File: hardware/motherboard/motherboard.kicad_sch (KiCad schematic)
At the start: 87 parts, among them J1 IMU Connector, J2 JST-VH, J3 JST-VH, J4 JST-PH, J5 USB C 2.0, J6 Conn_01x03_Pin, Q1 TSM7P06CP_ROG, Q2 TSM7P06CP_ROG, Q3 AO3400A, Q5 AO3400A, SW1 A, SW10 Right, SW11 Left, SW12 Up, SW13 Reset, SW2 B, SW3 X, SW4 Y, SW5 LB, SW6 RB, SW7 Start, SW8 Select, SW9 Down, U1 ESP32-S3-WROOM-1, U2 MCP73831-2-OT, U3 TPS75533KTTRG3, U4 TLV75709PDBV

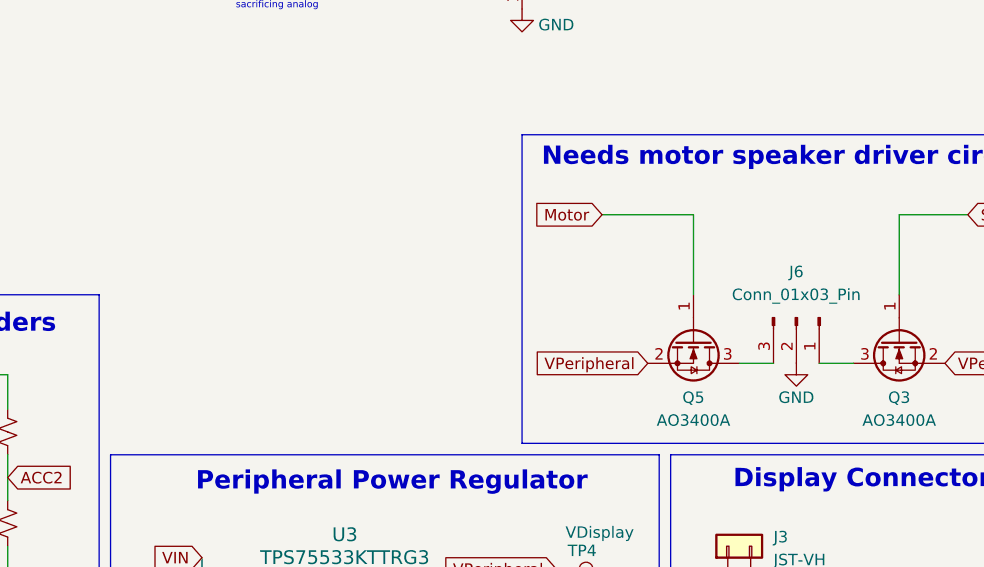
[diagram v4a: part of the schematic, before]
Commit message: Updated Mounting Holes
Made display holes M3

Matching hole pattern on motherboard to mount display.

Distributed 4, M3 mounting holes throuhout motherboard
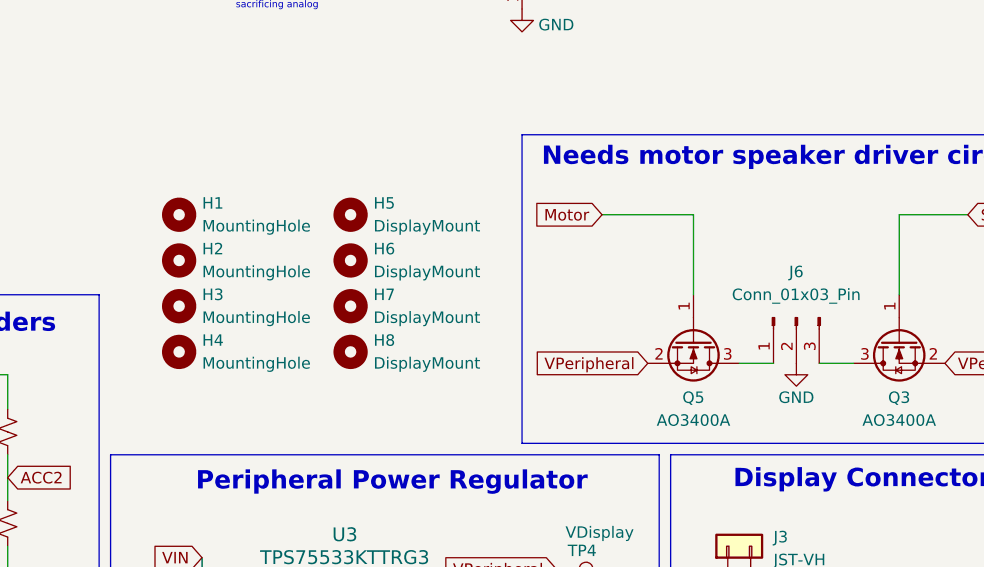
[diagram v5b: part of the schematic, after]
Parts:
- added H1, H2, H3, H4: MountingHole, MountingHole:MountingHole_3.2mm_M3_Pad, symbol Mechanical:MountingHole
- added H5, H6, H7, H8: DisplayMount, MountingHole:MountingHole_3.2mm_M3_Pad, symbol Mechanical:MountingHole
- J6: footprint Connector_JST:JST_EH_S3B-EH_1x03_P2.50mm_Horizontal -> Connector_JST:JST_PH_S3B-PH-K_1x03_P2.00mm_Horizontal
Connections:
- net at J6.1 (Pin_1): now also Q5.3 (D); no longer Q3.3 (D)
- net at J6.3 (Pin_3): now also Q3.3 (D); no longer Q5.3 (D)
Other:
- moved on the sheet: J6

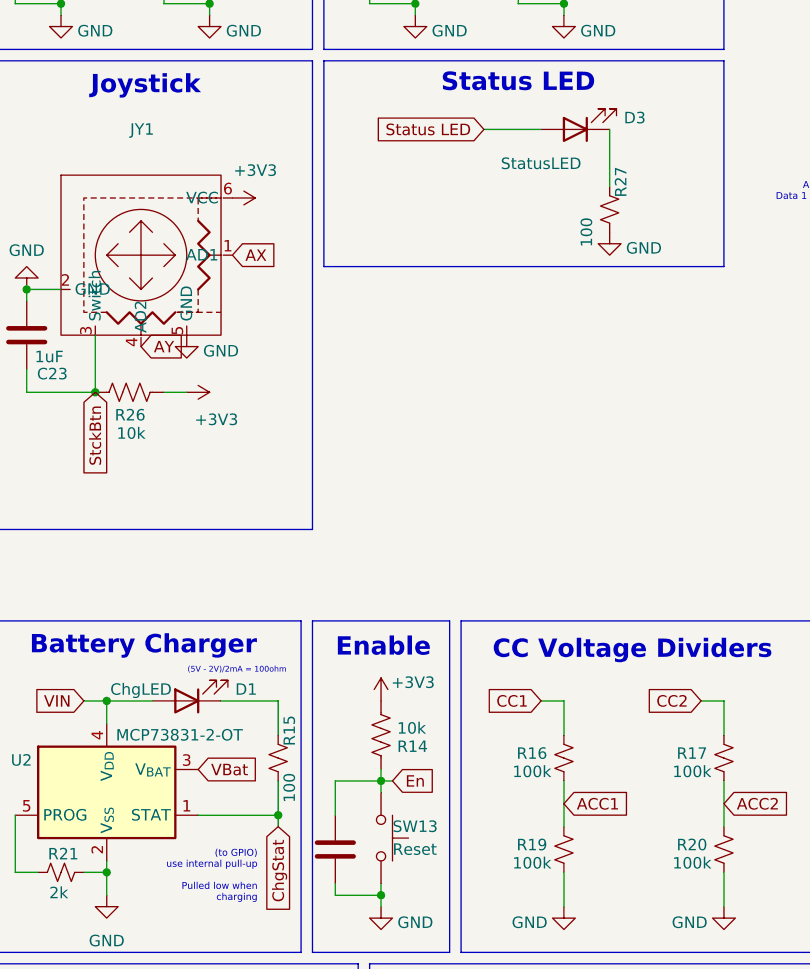
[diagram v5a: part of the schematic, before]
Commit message: Updated Motherboard and Minor Display Changes
Updated Joystick Position, Moved Display Board Port

other small fixes
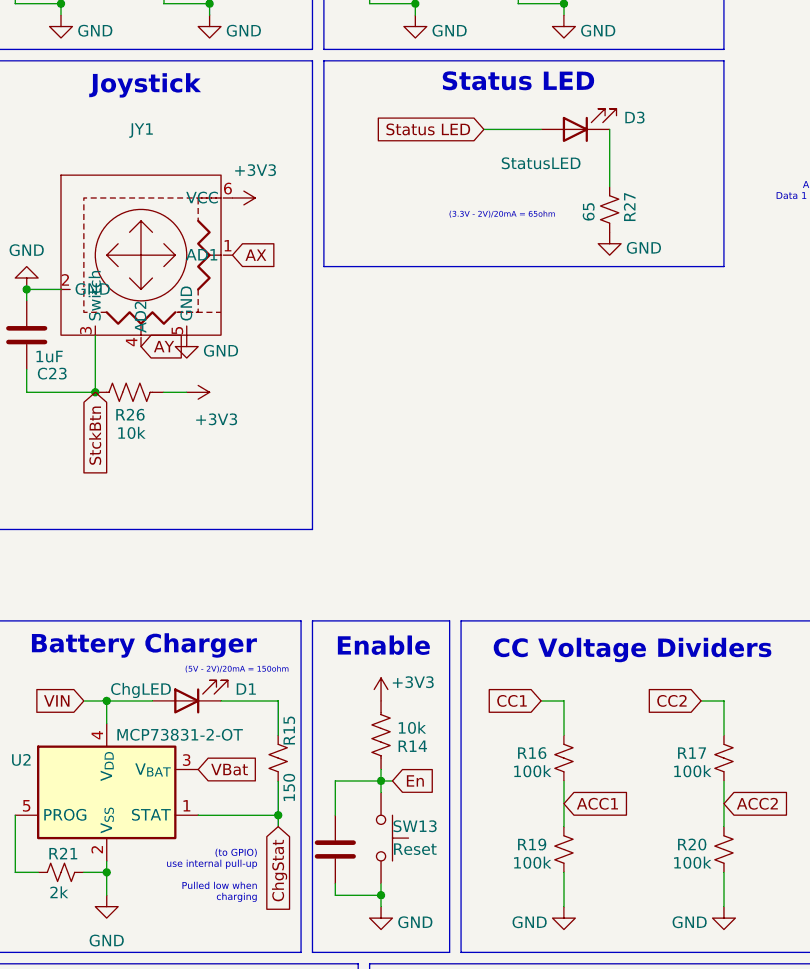
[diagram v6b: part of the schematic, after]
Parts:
- D1, D3: footprint LED_SMD:LED_1206_3216Metric -> LED_SMD:LED_1206_3216Metric_Pad1.42x1.75mm_HandSolder
- R15: value 100 -> 150
- R27: value 100 -> 65
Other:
- note added: "(3.3V - 2V)/20mA = 65ohm"
- note added: "(5V - 2V)/20mA = 150ohm"
- note removed: "(5V - 2V)/2mA = 100ohm"
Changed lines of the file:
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@@
 		)
 	)
-	(text "(5V - 2V)/2mA = 100ohm"
+	(text "(5V - 2V)/20mA = 150ohm"
 		(exclude_from_sim no)
 		(at 110.998 118.618 0)
@@
 		)
 	)
+	(text "(3.3V - 2V)/20mA = 65ohm"
+		(exclude_from_sim no)
+		(at 140.462 68.072 0)
+		(effects
+			(font
+				(size 0.635 0.635)
+			)
+		)
+	)
 	(text "A/B/X/Y"
 		(exclude_from_sim no)
@@
 			)
 		)
-		(property "Footprint" "LED_SMD:LED_1206_3216Metric"
+		(property "Footprint" "LED_SMD:LED_1206_3216Metric_Pad1.42x1.75mm_HandSolder"
 			(at 105.41 121.92 0)
 			(effects
@@
 			)
 		)
-		(property "Value" "100"
+		(property "Value" "150"
 			(at 116.84 131.572 90)
 			(effects
@@
 		(dnp no)
 		(property "Reference" "R27"
-			(at 153.67 64.262 90)
+			(at 154.686 67.056 90)
 			(effects
 				(font
@@
 			)
 		)
-		(property "Value" "100"
-			(at 149.86 69.85 90)
+		(property "Value" "65"
+			(at 150.114 67.564 90)
 			(effects
 				(font
@@
 			)
 		)
-		(property "Footprint" "LED_SMD:LED_1206_3216Metric"
+		(property "Footprint" "LED_SMD:LED_1206_3216Metric_Pad1.42x1.75mm_HandSolder"
 			(at 148.59 58.42 0)
 			(effects

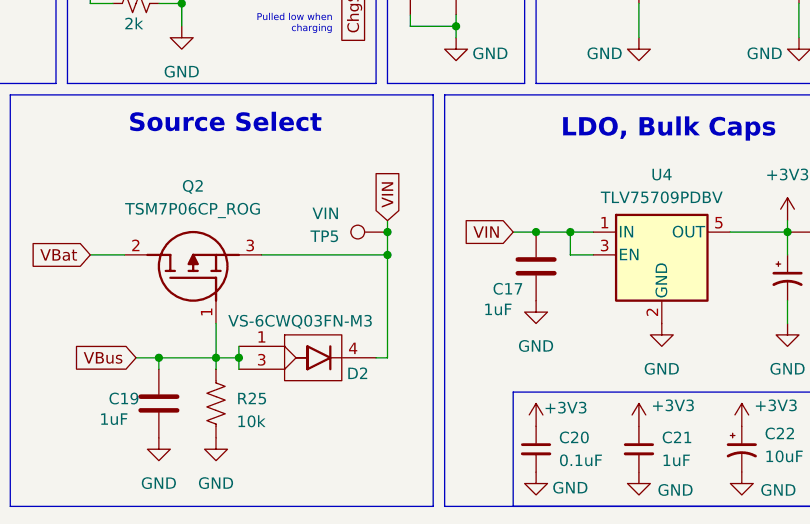
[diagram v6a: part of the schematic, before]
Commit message: ERC and DRC Checks
Made slight modifications to schematics and layouts to ensure ERCs and DRCs pass on both boards.

Made some exclusions for irrelevant warnings.
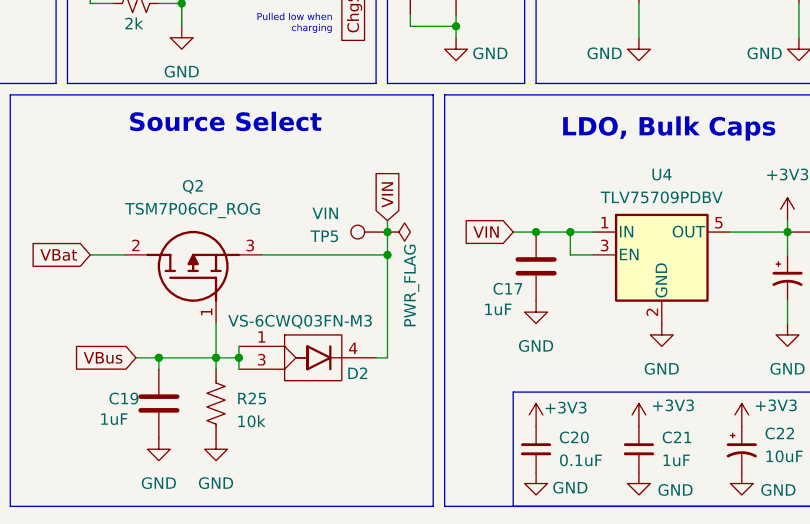
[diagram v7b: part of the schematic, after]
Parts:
- U3: footprint esp32_handheld:KTT5_6P22X6P86 -> KTT5_6P22X6P86
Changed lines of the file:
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@@
 	)
 	(symbol
+		(lib_id "power:PWR_FLAG")
+		(at 119.38 166.37 270)
+		(unit 1)
+		(exclude_from_sim no)
+		(in_bom yes)
+		(on_board yes)
+		(dnp no)
+		(property "Reference" "#FLG01"
+			(at 121.285 166.37 0)
+			(effects
+				(font
+					(size 1.27 1.27)
+				)
+				(hide yes)
+			)
+		)
+		(property "Value" "PWR_FLAG"
+			(at 121.92 167.64 0)
+			(effects
+				(font
+					(size 1.27 1.27)
+				)
+				(justify left)
+			)
+		)
+		(property "Footprint" ""
+			(at 119.38 166.37 0)
+			(effects
+				(font
+					(size 1.27 1.27)
+				)
+				(hide yes)
+			)
+		)
+		(property "Datasheet" "~"
+			(at 119.38 166.37 0)
+			(effects
+				(font
+					(size 1.27 1.27)
+				)
+				(hide yes)
+			)
+		)
+		(property "Description" "Special symbol for telling ERC where power comes from"
+			(at 119.38 166.37 0)
+			(effects
+				(font
+					(size 1.27 1.27)
+				)
+				(hide yes)
+			)
+		)
+		(pin "1"
+		)
+		(instances
+			(project ""
+				(path "/4bd92664-563a-4440-acf2-e22b0a15db62"
+					(reference "#FLG01")
+					(unit 1)
+				)
+			)
+		)
+	)
+	(symbol
 		(lib_id "power:GND")
 		(at 135.89 173.99 0)
@@
 	)
 	(symbol
+		(lib_name "Conn_01x02_1")
 		(lib_id "Connector_Generic:Conn_01x02")
 		(at 20.32 121.92 270)
@@
 			)
 		)
-		(property "Footprint" "esp32_handheld:KTT5_6P22X6P86"
+		(property "Footprint" "KTT5_6P22X6P86"
 			(at 183.896 131.064 0)
 			(effects

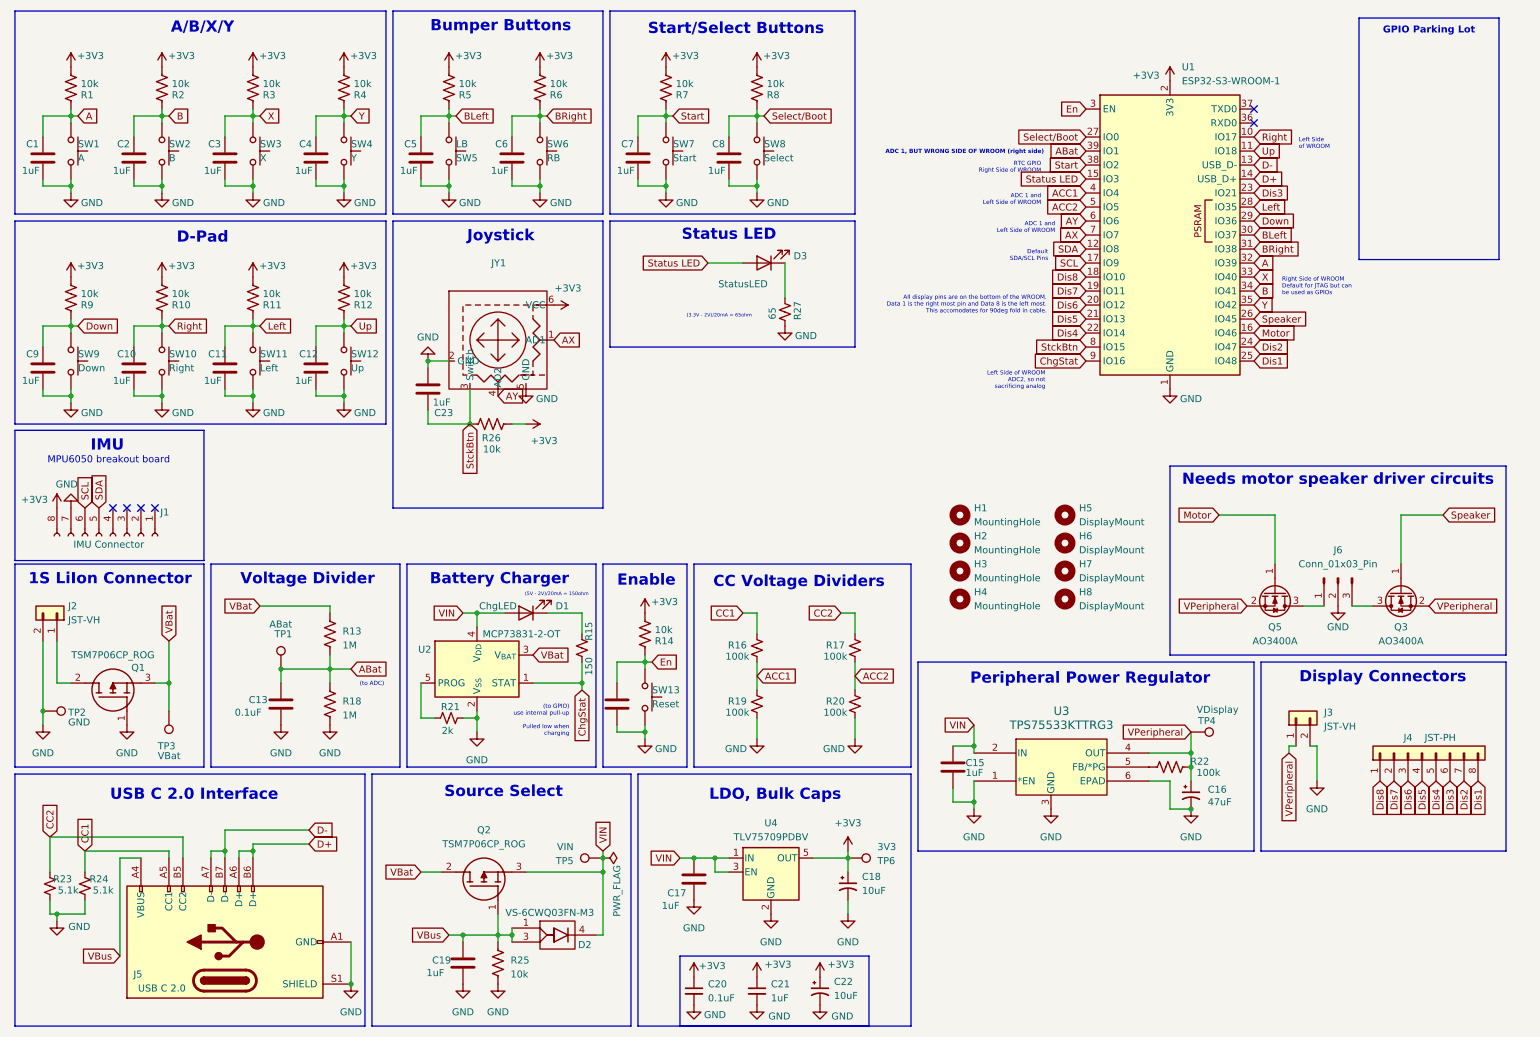
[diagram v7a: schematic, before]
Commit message: Quick modifications to add a high-side pmos switch between the battery and the display board
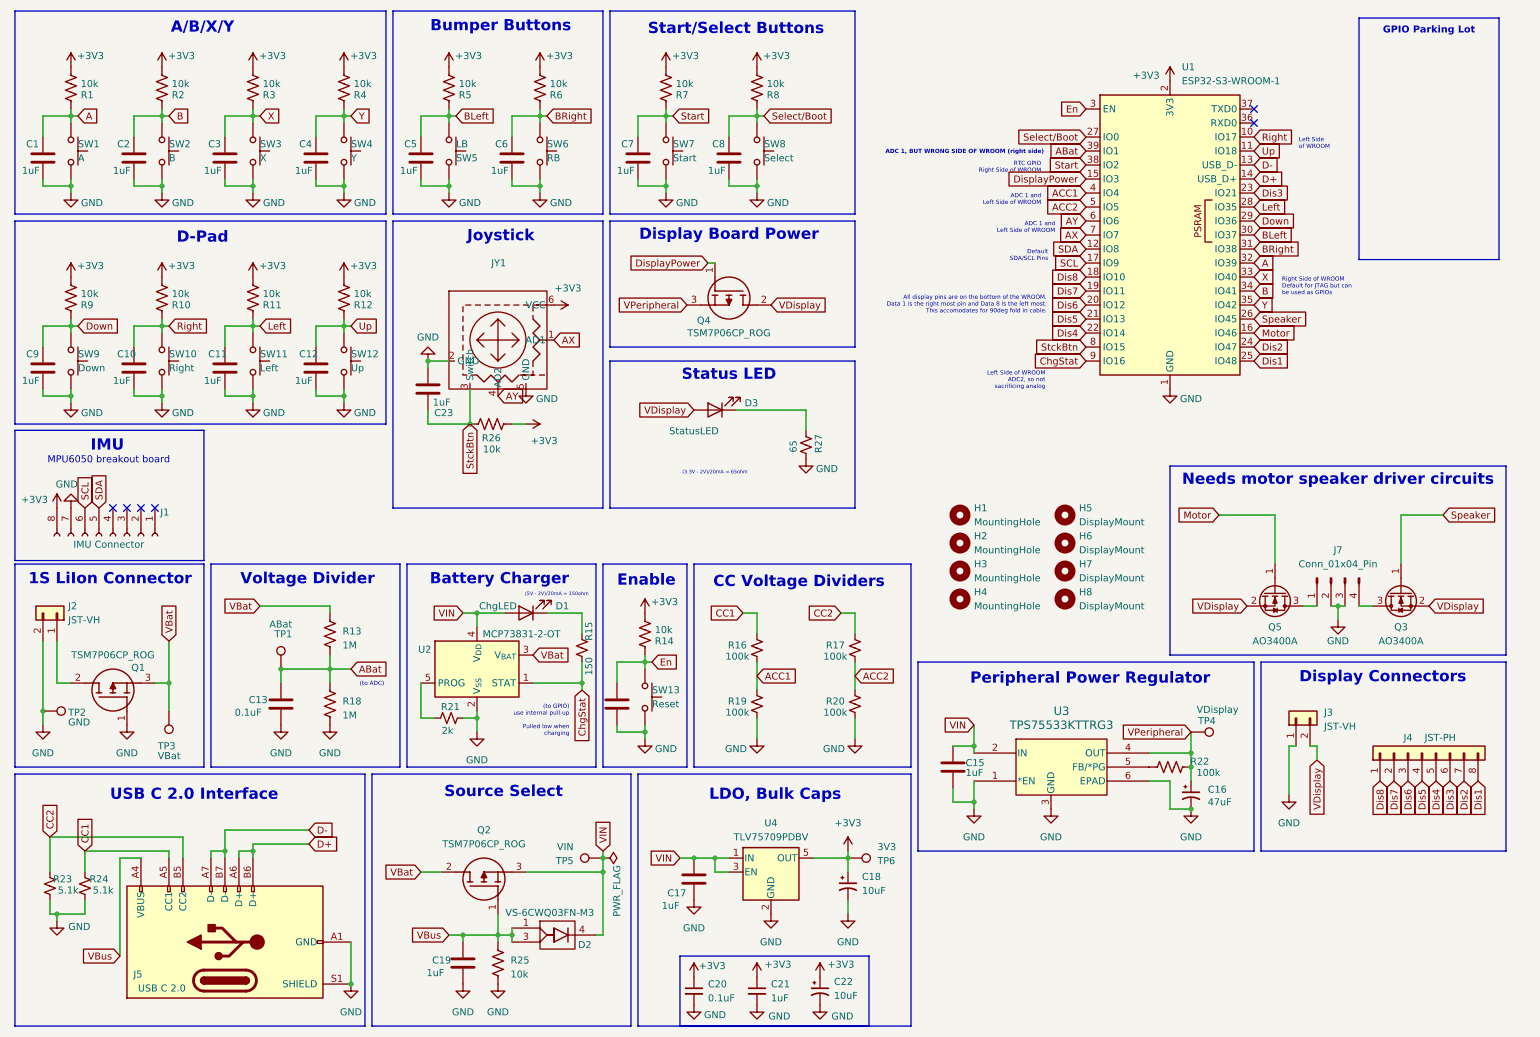
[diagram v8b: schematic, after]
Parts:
- removed J6: Conn_01x03_Pin, Connector_JST:JST_PH_S3B-PH-K_1x03_P2.00mm_Horizontal, symbol Connector:Conn_01x03_Pin
- added J7: Conn_01x04_Pin, Connector_JST:JST_PH_S4B-PH-K_1x04_P2.00mm_Horizontal, symbol Connector:Conn_01x04_Pin
- added Q4: TSM7P06CP_ROG, esp32_handheld:TRANS_TSM7P06CP_ROG, symbol esp32_handheld:TSM7P06CP_ROG
- U3: footprint KTT5_6P22X6P86 -> esp32_handheld:KTT5_6P22X6P86
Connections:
- net GND: now also J3.1 (Pin_1), J7.2 (Pin_2), J7.3 (Pin_3); no longer J3.2 (Pin_2)
- net VPeripheral: now also Q4.3 (S); no longer J3.1 (Pin_1), Q3.2 (S), Q5.2 (S)
- net at Q5.3 (D): now also J7.1 (Pin_1)
- net at Q3.3 (D): now also J7.4 (Pin_4)
- net Status LED renamed DisplayPower
- net DisplayPower: now also Q4.1 (G); no longer D3.2 (A)
- new net VDisplay: D3.2 (A), J3.2 (Pin_2), Q3.2 (S), Q4.2 (D), Q5.2 (S)
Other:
- note added: "Display Board Power"
- moved on the sheet: D3, R27
